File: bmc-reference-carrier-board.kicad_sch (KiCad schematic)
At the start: 0 parts

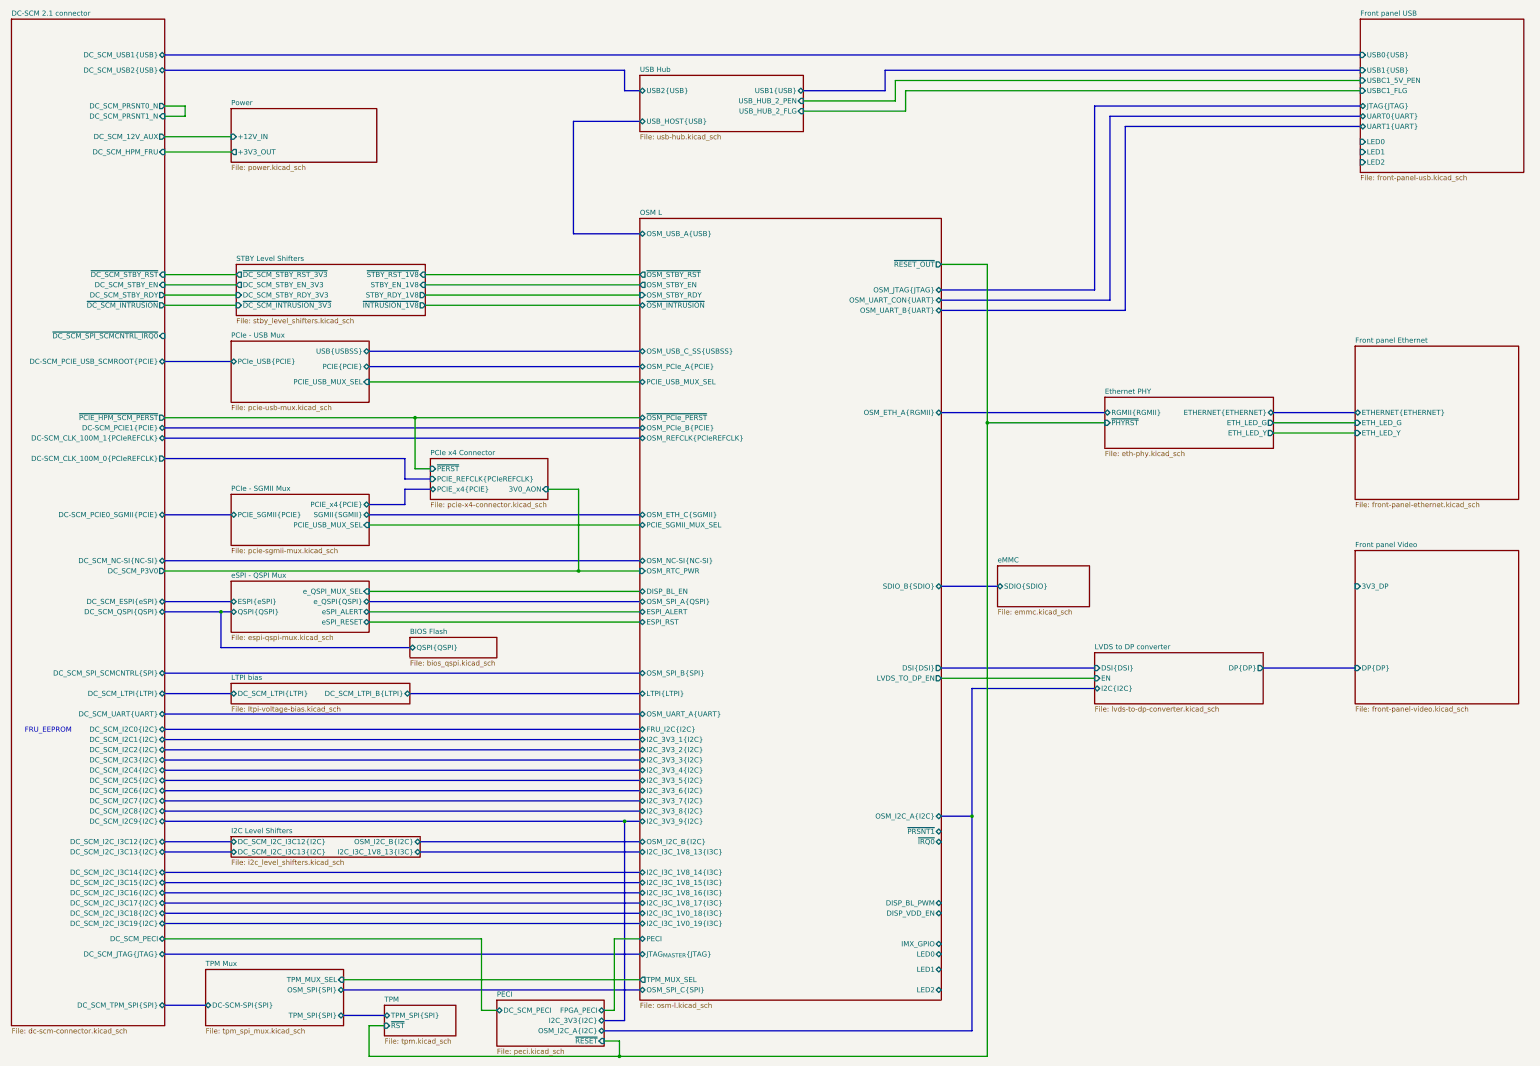
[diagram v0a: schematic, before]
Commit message: [#83336] Improved USB circuitry
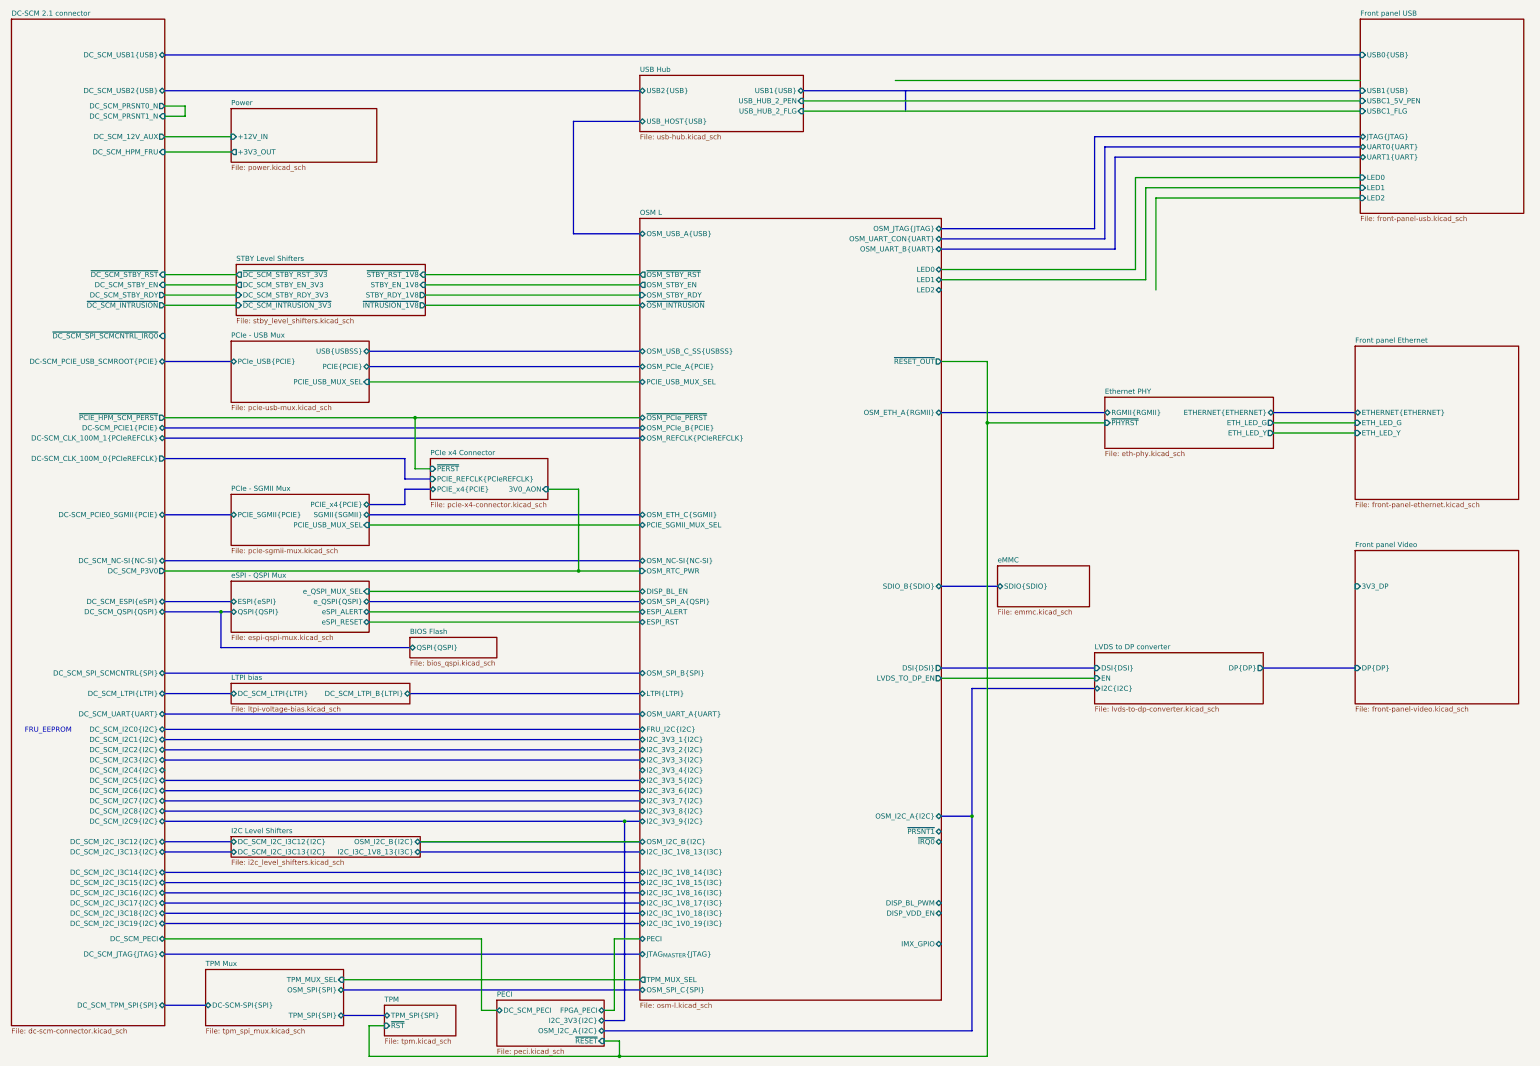
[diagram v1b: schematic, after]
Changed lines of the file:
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@@
 	(wire
 		(pts
+			(xy 355.6 67.31) (xy 302.26 67.31)
+		)
+		(stroke
+			(width 0)
+			(type default)
+		)
+	)
+	(wire
+		(pts
 			(xy 58.42 46.99) (xy 63.5 46.99)
 		)
@@
 	(bus
 		(pts
-			(xy 293.37 95.25) (xy 251.46 95.25)
+			(xy 292.1 80.01) (xy 251.46 80.01)
 		)
 		(stroke
@@
 		)
 	)
+	(wire
+		(pts
+			(xy 304.8 92.71) (xy 304.8 69.85)
+		)
+		(stroke
+			(width 0)
+			(type default)
+		)
+	)
 	(bus
 		(pts
@@
 	(wire
 		(pts
+			(xy 302.26 90.17) (xy 251.46 90.17)
+		)
+		(stroke
+			(width 0)
+			(type default)
+		)
+	)
+	(wire
+		(pts
 			(xy 58.42 58.42) (xy 74.93 58.42)
 		)
@@
 	(bus
 		(pts
-			(xy 297.18 52.07) (xy 355.6 52.07)
+			(xy 294.64 59.69) (xy 355.6 59.69)
 		)
 		(stroke
@@
 	(bus
 		(pts
-			(xy 289.56 92.71) (xy 289.56 46.99)
+			(xy 289.56 77.47) (xy 289.56 54.61)
 		)
 		(stroke
@@
 	(bus
 		(pts
-			(xy 172.72 43.18) (xy 176.53 43.18)
-		)
-		(stroke
-			(width 0)
-			(type default)
-		)
-	)
-	(bus
-		(pts
 			(xy 58.42 237.49) (xy 176.53 237.49)
 		)
@@
 	(wire
 		(pts
-			(xy 217.17 45.72) (xy 240.03 45.72)
+			(xy 217.17 45.72) (xy 355.6 45.72)
 		)
 		(stroke
@@
 	(bus
 		(pts
-			(xy 355.6 49.53) (xy 293.37 49.53)
+			(xy 355.6 57.15) (xy 292.1 57.15)
 		)
 		(stroke
@@
 		)
 	)
-	(bus
-		(pts
-			(xy 172.72 38.1) (xy 172.72 43.18)
-		)
-		(stroke
-			(width 0)
-			(type default)
-		)
-	)
 	(wire
 		(pts
-			(xy 217.17 48.26) (xy 242.57 48.26)
+			(xy 217.17 48.26) (xy 355.6 48.26)
 		)
 		(stroke
@@
 		)
 	)
-	(bus
+	(wire
 		(pts
-			(xy 237.49 38.1) (xy 355.6 38.1)
+			(xy 251.46 110.49) (xy 262.89 110.49)
 		)
 		(stroke
@@
 	(wire
 		(pts
-			(xy 251.46 86.36) (xy 262.89 86.36)
+			(xy 109.22 167.64) (xy 176.53 167.64)
 		)
 		(stroke
@@
 	(bus
 		(pts
-			(xy 237.49 38.1) (xy 237.49 43.18)
+			(xy 58.42 110.49) (xy 74.93 110.49)
 		)
 		(stroke
@@
 	(wire
 		(pts
-			(xy 109.22 167.64) (xy 176.53 167.64)
-		)
-		(stroke
-			(width 0)
-			(type default)
-		)
-	)
-	(bus
-		(pts
-			(xy 58.42 110.49) (xy 74.93 110.49)
+			(xy 299.72 64.77) (xy 355.6 64.77)
 		)
 		(stroke
@@
 	(bus
 		(pts
-			(xy 172.72 38.1) (xy 58.42 38.1)
+			(xy 58.42 43.18) (xy 176.53 43.18)
 		)
 		(stroke
@@
 		)
 	)
+	(wire
+		(pts
+			(xy 304.8 69.85) (xy 355.6 69.85)
+		)
+		(stroke
+			(width 0)
+			(type default)
+		)
+	)
 	(bus
 		(pts
-			(xy 217.17 43.18) (xy 237.49 43.18)
+			(xy 217.17 43.18) (xy 355.6 43.18)
 		)
 		(stroke
@@
 		)
 	)
+	(wire
+		(pts
+			(xy 251.46 87.63) (xy 299.72 87.63)
+		)
+		(stroke
+			(width 0)
+			(type default)
+		)
+	)
+	(wire
+		(pts
+			(xy 302.26 67.31) (xy 302.26 90.17)
+		)
+		(stroke
+			(width 0)
+			(type default)
+		)
+	)
 	(bus
 		(pts
@@
 	(bus
 		(pts
-			(xy 251.46 97.79) (xy 297.18 97.79)
+			(xy 251.46 82.55) (xy 294.64 82.55)
 		)
 		(stroke
@@
 		)
 	)
-	(bus
+	(wire
 		(pts
-			(xy 58.42 245.11) (xy 176.53 245.11)
+			(xy 299.72 87.63) (xy 299.72 64.77)
 		)
 		(stroke
@@
 	(bus
 		(pts
-			(xy 119.38 193.04) (xy 176.53 193.04)
+			(xy 58.42 245.11) (xy 176.53 245.11)
 		)
 		(stroke
@@
 		)
 	)
-	(wire
+	(bus
 		(pts
-			(xy 242.57 43.18) (xy 355.6 43.18)
+			(xy 119.38 193.04) (xy 176.53 193.04)
 		)
 		(stroke
@@
 	(bus
 		(pts
-			(xy 289.56 46.99) (xy 355.6 46.99)
+			(xy 289.56 54.61) (xy 355.6 54.61)
 		)
 		(stroke
@@
 	(wire
 		(pts
-			(xy 262.89 86.36) (xy 262.89 125.73)
+			(xy 262.89 110.49) (xy 262.89 125.73)
 		)
 		(stroke
@@
 		)
 	)
-	(bus
+	(wire
 		(pts
 			(xy 121.92 229.87) (xy 176.53 229.87)
@@
 		)
 	)
-	(wire
+	(bus
 		(pts
 			(xy 242.57 48.26) (xy 242.57 43.18)
@@
 		)
 	)
-	(wire
+	(bus
 		(pts
-			(xy 102.87 264.16) (xy 176.53 264.16)
+			(xy 121.92 229.87) (xy 176.53 229.87)
 		)
 		(stroke
@@
 		)
 	)
-	(bus
+	(wire
 		(pts
-			(xy 58.42 212.09) (xy 176.53 212.09)
+			(xy 102.87 264.16) (xy 176.53 264.16)
 		)
 		(stroke
@@
 	(bus
 		(pts
-			(xy 293.37 49.53) (xy 293.37 95.25)
-		)
-		(stroke
-			(width 0)
-			(type default)
-		)
-	)
-	(wire
-		(pts
-			(xy 240.03 45.72) (xy 240.03 40.64)
+			(xy 292.1 57.15) (xy 292.1 80.01)
 		)
 		(stroke
@@
 	(bus
 		(pts
-			(xy 297.18 97.79) (xy 297.18 52.07)
+			(xy 294.64 82.55) (xy 294.64 59.69)
 		)
 		(stroke
@@
 	(bus
 		(pts
-			(xy 251.46 92.71) (xy 289.56 92.71)
+			(xy 251.46 77.47) (xy 289.56 77.47)
 		)
 		(stroke
@@
 	(sheet
 		(at 355.6 25.4)
-		(size 40.64 38.1)
+		(size 40.64 48.26)
 		(exclude_from_sim no)
 		(in_bom yes)
@@
 		)
 		(property "Sheetfile" "front-panel-usb.kicad_sch"
-			(at 355.6 64.0846 0)
+			(at 355.6 74.2446 0)
 			(effects
 				(font
@@
 		)
 		(pin "USB1{USB}" input
-			(at 355.6 38.1 180)
+			(at 355.6 43.18 180)
 			(effects
 				(font
@@
 		)
 		(pin "JTAG{JTAG}" bidirectional
-			(at 355.6 46.99 180)
+			(at 355.6 54.61 180)
 			(effects
 				(font
@@
 		)
 		(pin "LED0" input
-			(at 355.6 55.88 180)
+			(at 355.6 64.77 180)
 			(effects
 				(font
@@
 		)
 		(pin "LED1" input
-			(at 355.6 58.42 180)
+			(at 355.6 67.31 180)
 			(effects
 				(font
@@
 		)
 		(pin "UART0{UART}" bidirectional
-			(at 355.6 49.53 180)
+			(at 355.6 57.15 180)
 			(effects
 				(font
@@
 		)
 		(pin "UART1{UART}" bidirectional
-			(at 355.6 52.07 180)
+			(at 355.6 59.69 180)
 			(effects
 				(font
@@
 		)
 		(pin "LED2" input
-			(at 355.6 60.96 180)
+			(at 355.6 69.85 180)
 			(effects
 				(font
@@
 		)
 		(pin "USBC1_5V_PEN" input
-			(at 355.6 40.64 180)
+			(at 355.6 45.72 180)
 			(effects
 				(font
@@
 		)
 		(pin "USBC1_FLG" input
-			(at 355.6 43.18 180)
+			(at 355.6 48.26 180)
 			(effects
 				(font
@@
 		)
 		(pin "OSM_JTAG{JTAG}" bidirectional
-			(at 251.46 92.71 0)
+			(at 251.46 77.47 0)
 			(effects
 				(font
@@
 		)
 		(pin "OSM_UART_B{UART}" bidirectional
-			(at 251.46 97.79 0)
+			(at 251.46 82.55 0)
 			(effects
 				(font
@@
 		)
 		(pin "OSM_UART_CON{UART}" bidirectional
-			(at 251.46 95.25 0)
+			(at 251.46 80.01 0)
 			(effects
 				(font
@@
 		)
 		(pin "LED0" bidirectional
-			(at 251.46 257.81 0)
+			(at 251.46 87.63 0)
 			(effects
 				(font
@@
 		)
 		(pin "LED1" bidirectional
-			(at 251.46 261.62 0)
+			(at 251.46 90.17 0)
 			(effects
 				(font
@@
 		)
 		(pin "LED2" bidirectional
-			(at 251.46 266.7 0)
+			(at 251.46 92.71 0)
 			(effects
 				(font
@@
 		)
 		(pin "~{RESET_OUT}" output
-			(at 251.46 86.36 0)
+			(at 251.46 110.49 0)
 			(effects
 				(font
@@
 		)
 		(pin "DC_SCM_USB2{USB}" bidirectional
-			(at 58.42 38.1 0)
+			(at 58.42 43.18 0)
 			(effects
 				(font

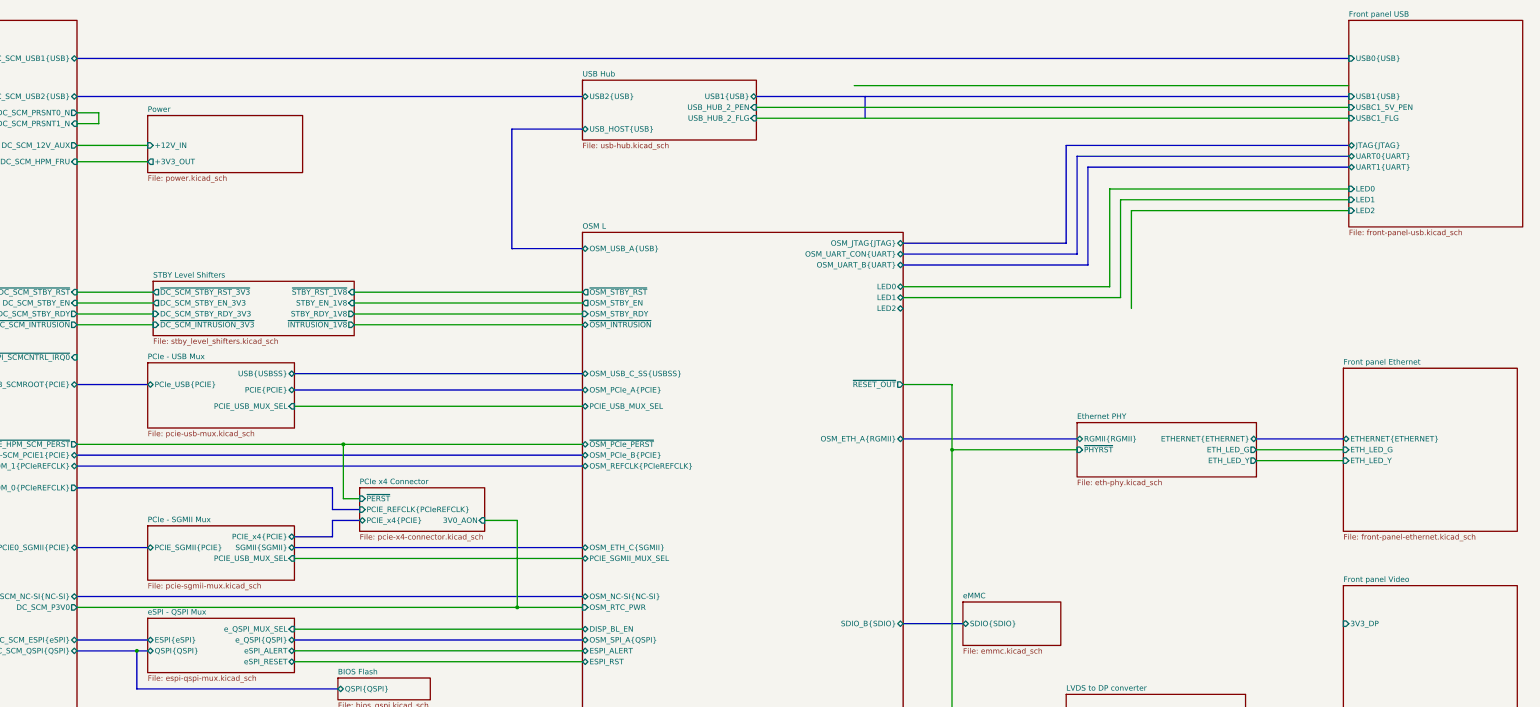
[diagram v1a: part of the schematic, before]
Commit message: [#83336] Small front panel interface fixes
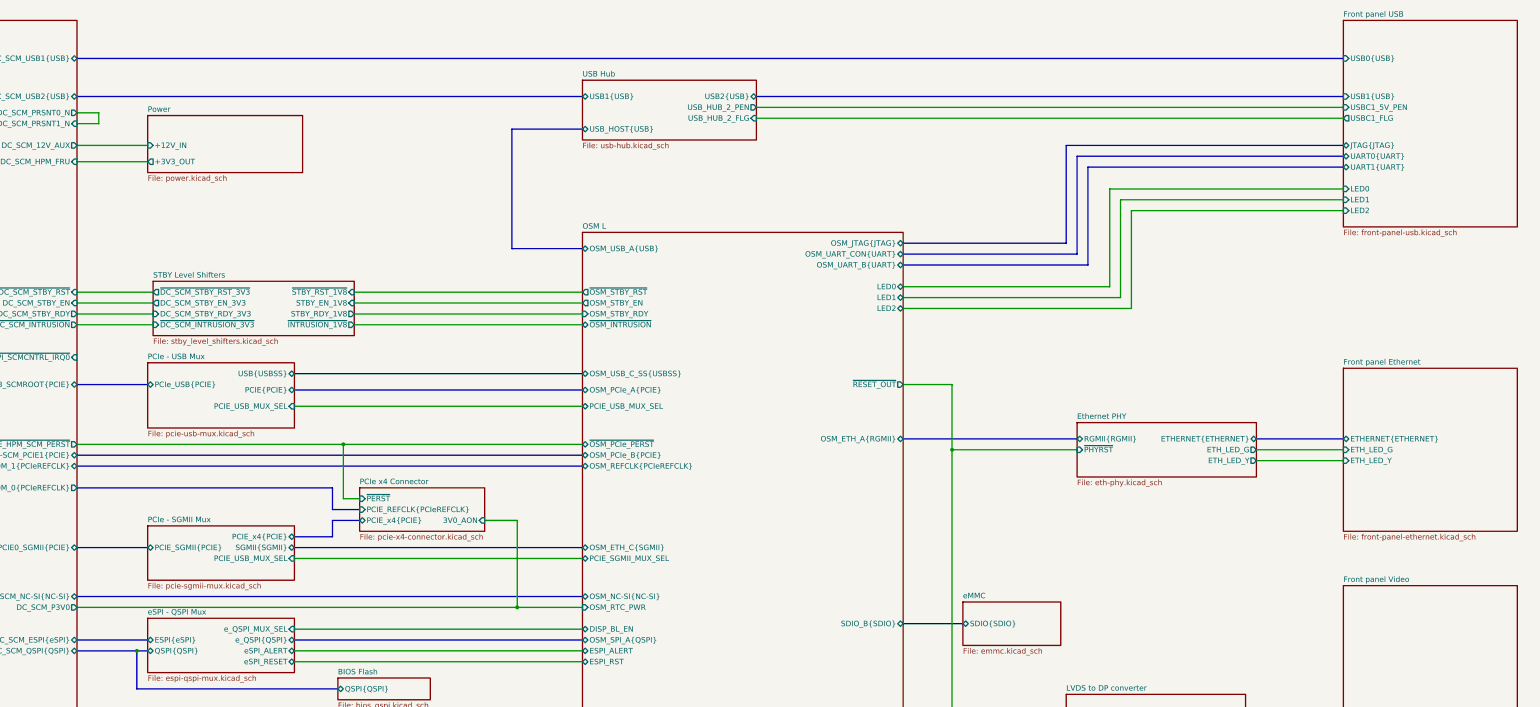
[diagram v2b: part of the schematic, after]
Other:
- sheet Front panel Video ports: added none; removed 3V3_DP
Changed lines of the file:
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@@
 	(wire
 		(pts
-			(xy 355.6 67.31) (xy 302.26 67.31)
+			(xy 354.33 67.31) (xy 302.26 67.31)
 		)
 		(stroke
@@
 		)
 	)
+	(wire
+		(pts
+			(xy 251.46 92.71) (xy 304.8 92.71)
+		)
+		(stroke
+			(width 0)
+			(type default)
+		)
+	)
 	(bus
 		(pts
@@
 	(bus
 		(pts
-			(xy 294.64 59.69) (xy 355.6 59.69)
+			(xy 294.64 59.69) (xy 354.33 59.69)
 		)
 		(stroke
@@
 	(wire
 		(pts
-			(xy 217.17 45.72) (xy 355.6 45.72)
+			(xy 217.17 45.72) (xy 354.33 45.72)
 		)
 		(stroke
@@
 	(bus
 		(pts
-			(xy 355.6 57.15) (xy 292.1 57.15)
+			(xy 354.33 57.15) (xy 292.1 57.15)
 		)
 		(stroke
@@
 	(wire
 		(pts
-			(xy 217.17 48.26) (xy 355.6 48.26)
+			(xy 217.17 48.26) (xy 354.33 48.26)
 		)
 		(stroke
@@
 	(wire
 		(pts
-			(xy 299.72 64.77) (xy 355.6 64.77)
+			(xy 299.72 64.77) (xy 354.33 64.77)
 		)
 		(stroke
@@
 	(wire
 		(pts
-			(xy 304.8 69.85) (xy 355.6 69.85)
-		)
-		(stroke
-			(width 0)
-			(type default)
-		)
-	)
-	(bus
-		(pts
-			(xy 217.17 43.18) (xy 355.6 43.18)
+			(xy 304.8 69.85) (xy 354.33 69.85)
+		)
+		(stroke
+			(width 0)
+			(type default)
+		)
+	)
+	(bus
+		(pts
+			(xy 217.17 43.18) (xy 354.33 43.18)
 		)
 		(stroke
@@
 	(bus
 		(pts
-			(xy 289.56 54.61) (xy 355.6 54.61)
+			(xy 289.56 54.61) (xy 354.33 54.61)
 		)
 		(stroke
@@
 	(bus
 		(pts
-			(xy 242.57 48.26) (xy 242.57 43.18)
-		)
-		(stroke
-			(width 0)
-			(type default)
-		)
-	)
-	(bus
-		(pts
 			(xy 121.92 229.87) (xy 176.53 229.87)
 		)
@@
 	(wire
 		(pts
-			(xy 240.03 40.64) (xy 355.6 40.64)
-		)
-		(stroke
-			(width 0)
-			(type default)
-		)
-	)
-	(wire
-		(pts
 			(xy 123.19 91.44) (xy 176.53 91.44)
 		)
@@
 	(bus
 		(pts
-			(xy 58.42 34.29) (xy 355.6 34.29)
+			(xy 58.42 34.29) (xy 354.33 34.29)
 		)
 		(stroke
@@
 			)
 		)
-		(pin "USB1{USB}" bidirectional
-			(at 217.17 43.18 0)
-			(effects
-				(font
-					(size 1.27 1.27)
-				)
-				(justify right)
-			)
-		)
-		(pin "USB2{USB}" bidirectional
-			(at 176.53 43.18 180)
-			(effects
-				(font
-					(size 1.27 1.27)
-				)
-				(justify left)
-			)
-		)
 		(pin "USB_HUB_2_FLG" input
 			(at 217.17 48.26 0)
@@
 			)
 		)
-		(pin "USB_HUB_2_PEN" input
+		(pin "USB_HUB_2_PEN" output
 			(at 217.17 45.72 0)
+			(effects
+				(font
+					(size 1.27 1.27)
+				)
+				(justify right)
+			)
+		)
+		(pin "USB1{USB}" bidirectional
+			(at 176.53 43.18 180)
+			(effects
+				(font
+					(size 1.27 1.27)
+				)
+				(justify left)
+			)
+		)
+		(pin "USB2{USB}" bidirectional
+			(at 217.17 43.18 0)
 			(effects
 				(font
@@
 	)
 	(sheet
-		(at 355.6 25.4)
+		(at 354.33 25.4)
 		(size 40.64 48.26)
 		(exclude_from_sim no)
@@
 		)
 		(property "Sheetname" "Front panel USB"
-			(at 355.6 24.6884 0)
+			(at 354.33 24.6884 0)
 			(effects
 				(font
@@
 		)
 		(property "Sheetfile" "front-panel-usb.kicad_sch"
-			(at 355.6 74.2446 0)
+			(at 354.33 74.2446 0)
 			(effects
 				(font
@@
 		)
 		(pin "USB0{USB}" input
-			(at 355.6 34.29 180)
+			(at 354.33 34.29 180)
 			(effects
 				(font
@@
 		)
 		(pin "USB1{USB}" input
-			(at 355.6 43.18 180)
+			(at 354.33 43.18 180)
 			(effects
 				(font
@@
 		)
 		(pin "JTAG{JTAG}" bidirectional
-			(at 355.6 54.61 180)
+			(at 354.33 54.61 180)
 			(effects
 				(font
@@
 		)
 		(pin "LED0" input
-			(at 355.6 64.77 180)
+			(at 354.33 64.77 180)
 			(effects
 				(font
@@
 		)
 		(pin "LED1" input
-			(at 355.6 67.31 180)
+			(at 354.33 67.31 180)
 			(effects
 				(font
@@
 		)
 		(pin "UART0{UART}" bidirectional
-			(at 355.6 57.15 180)
+			(at 354.33 57.15 180)
 			(effects
 				(font
@@
 		)
 		(pin "UART1{UART}" bidirectional
-			(at 355.6 59.69 180)
+			(at 354.33 59.69 180)
 			(effects
 				(font
@@
 		)
 		(pin "LED2" input
-			(at 355.6 69.85 180)
+			(at 354.33 69.85 180)
 			(effects
 				(font
@@
 		)
 		(pin "USBC1_5V_PEN" input
-			(at 355.6 45.72 180)
+			(at 354.33 45.72 180)
 			(effects
 				(font
@@
 			)
 		)
-		(pin "USBC1_FLG" input
-			(at 355.6 48.26 180)
+		(pin "USBC1_FLG" output
+			(at 354.33 48.26 180)
 			(effects
 				(font
@@
 			(effects
 				(font
-					(size 1.27 1.27)
-				)
-				(justify left)
-			)
-		)
-		(pin "3V3_DP" input
-			(at 354.33 166.37 180)
-			(effects
-				(font
